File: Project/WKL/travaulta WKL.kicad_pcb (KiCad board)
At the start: 4 copper layers, 208.3 x 75.8 mm, 107 parts, among them J1 ARGB, SW1 EC_SW, SW10 EC_SW, SW11 EC_SW, SW12 EC_SW, SW13 EC_SW, SW14 EC_SW, SW15 EC_SW, SW16 EC_SW, SW17 EC_SW, SW18 EC_SW, SW19 EC_SW, SW2 EC_SW, SW20 EC_SW, SW21 EC_SW, SW22 EC_SW, SW23 EC_SW, SW24 EC_SW, SW25 EC_SW, SW26 EC_SW, SW27 EC_SW, SW28 EC_SW, SW29 EC_SW, SW3 EC_SW, SW30 EC_SW, SW31 EC_SW, SW32 EC_SW, SW33 EC_SW, SW34 EC_SW, SW35 EC_SW, SW36 EC_SW, SW37 EC_SW, SW38 BOOT0, SW4 EC_SW, SW5 EC_SW, SW6 EC_SW, SW7 EC_SW, SW8 EC_SW, SW9 EC_SW, U1 STM32F401CBUx, U2 XC6206PxxxMR, U3 74HC4051, U4 74HC4051, U5 OPA350, Y1 8 MHz

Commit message: backup
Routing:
- net GND: track 46.9 -> 54.4 mm, vias 435 -> 431
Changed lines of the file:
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@@
   (via (at 163.576 76.2) (size 0.8) (drill 0.4) (layers "F.Cu" "B.Cu") (net 1))
   (via (at 195.012249 65.997905) (size 0.8) (drill 0.4) (layers "F.Cu" "B.Cu") (free) (net 1))
-  (via (at 153.288724 110.807639) (size 0.8) (drill 0.4) (layers "F.Cu" "B.Cu") (net 1))
   (via (at 111.531688 103.066962) (size 0.8) (drill 0.4) (layers "F.Cu" "B.Cu") (free) (net 1))
   (via (at 71.700833 102.228857) (size 0.8) (drill 0.4) (layers "F.Cu" "B.Cu") (free) (net 1))
@@
   (via (at 118.067619 104.395436) (size 0.8) (drill 0.4) (layers "F.Cu" "B.Cu") (free) (net 1))
   (via (at 223.514768 103.879942) (size 0.8) (drill 0.4) (layers "F.Cu" "B.Cu") (free) (net 1))
-  (via (at 150.5501 110.815963) (size 0.8) (drill 0.4) (layers "F.Cu" "B.Cu") (net 1))
   (via (at 78.556941 103.85914) (size 0.8) (drill 0.4) (layers "F.Cu" "B.Cu") (free) (net 1))
   (via (at 237.353345 102.760391) (size 0.8) (drill 0.4) (layers "F.Cu" "B.Cu") (free) (net 1))
@@
   (via (at 215.79072 65.997413) (size 0.8) (drill 0.4) (layers "F.Cu" "B.Cu") (free) (net 1))
   (via (at 139.953601 68.350091) (size 0.8) (drill 0.4) (layers "F.Cu" "B.Cu") (free) (net 1))
-  (via (at 153.346 115.062) (size 0.8) (drill 0.4) (layers "F.Cu" "B.Cu") (net 1))
   (via (at 87.653038 51.101306) (size 0.8) (drill 0.4) (layers "F.Cu" "B.Cu") (net 1))
   (via (at 84.074 69.85) (size 0.8) (drill 0.4) (layers "F.Cu" "B.Cu") (free) (net 1))
   (via (at 151.425252 121.036363) (size 0.8) (drill 0.4) (layers "F.Cu" "B.Cu") (free) (net 1))
   (via (at 184.94375 106.3625) (size 0.8) (drill 0.4) (layers "F.Cu" "B.Cu") (net 1))
-  (via (at 150.425 115.062) (size 0.8) (drill 0.4) (layers "F.Cu" "B.Cu") (net 1))
   (segment (start 85.75 53.624) (end 86.81 53.624) (width 0.25) (layer "B.Cu") (net 1))
   (segment (start 157.41 114.683) (end 158.047 114.683) (width 0.25) (layer "B.Cu") (net 1))
   (segment (start 86.81 53.624) (end 87.67 52.764) (width 0.25) (layer "B.Cu") (net 1))
+  (segment (start 154.904 109.4655) (end 154.904 110.653) (width 0.25) (layer "B.Cu") (net 1))
   (segment (start 86.87 50.318268) (end 86.87 48.44375) (width 0.25) (layer "B.Cu") (net 1))
   (segment (start 87.653038 51.101306) (end 86.87 50.318268) (width 0.25) (layer "B.Cu") (net 1))
@@
   (segment (start 77.43 52.764) (end 77.43 51.094) (width 0.25) (layer "B.Cu") (net 1))
   (segment (start 151.896 116.3405) (end 151.896 113.591) (width 0.25) (layer "B.Cu") (net 1))
-  (segment (start 154.851186 115.15718) (end 154.701186 115.00718) (width 0.25) (layer "B.Cu") (net 1))
   (segment (start 78.29 53.624) (end 77.43 52.764) (width 0.25) (layer "B.Cu") (net 1))
   (segment (start 149.04 118.491) (end 149.031 118.5) (width 0.25) (layer "B.Cu") (net 1))
   (segment (start 188.33834 107.55242) (end 188.33834 106.58209) (width 0.25) (layer "B.Cu") (net 1))
   (segment (start 82.903 69.85) (end 84.074 69.85) (width 0.25) (layer "B.Cu") (net 1))
-  (segment (start 154.889279 109.405399) (end 154.889279 110.592899) (width 0.25) (layer "B.Cu") (net 1))
   (segment (start 77.77875 48.895) (end 75.692 48.895) (width 0.25) (layer "B.Cu") (net 1))
   (segment (start 188.33834 106.58209) (end 188.08319 106.32694) (width 0.25) (layer "B.Cu") (net 1))
@@
   (segment (start 77.43 51.094) (end 78.23 50.294) (width 0.25) (layer "B.Cu") (net 1))
   (segment (start 84.201 56.35625) (end 84.201 57.283328) (width 0.25) (layer "B.Cu") (net 1))
-  (segment (start 150.4001 110.665963) (end 150.5501 110.815963) (width 0.25) (layer "B.Cu") (net 1))
+  (segment (start 156.0915 115.153) (end 154.904 115.153) (width 0.25) (layer "B.Cu") (net 1))
   (segment (start 187.12434 106.32694) (end 184.97931 106.32694) (width 0.25) (layer "B.Cu") (net 1))
   (segment (start 151.896 116.3405) (end 151.896 118.233) (width 0.25) (layer "B.Cu") (net 1))
   (segment (start 78.23 50.294) (end 78.23 48.44375) (width 0.25) (layer "B.Cu") (net 1))
+  (segment (start 149.2165 110.653) (end 150.334 110.653) (width 0.25) (layer "B.Cu") (net 1))
   (segment (start 187.12434 107.62742) (end 188.26334 107.62742) (width 0.25) (layer "B.Cu") (net 1))
   (segment (start 79.35 53.624) (end 78.29 53.624) (width 0.25) (layer "B.Cu") (net 1))
@@
   (segment (start 87.67 52.764) (end 87.67 51.118268) (width 0.25) (layer "B.Cu") (net 1))
   (segment (start 158.299 115.635994) (end 158.271 115.663994) (width 0.25) (layer "B.Cu") (net 1))
-  (segment (start 150.5501 110.815963) (end 150.387137 110.653) (width 0.25) (layer "B.Cu") (net 1))
   (segment (start 78.23 48.44375) (end 77.77875 48.895) (width 0.25) (layer "B.Cu") (net 1))
+  (segment (start 154.904 110.653) (end 152.654 112.903) (width 0.25) (layer "B.Cu") (net 1))
   (segment (start 184.97931 106.32694) (end 184.94375 106.3625) (width 0.25) (layer "B.Cu") (net 1))
   (segment (start 87.32125 48.895) (end 89.408 48.895) (width 0.25) (layer "B.Cu") (net 1))
-  (segment (start 156.038686 115.15718) (end 154.851186 115.15718) (width 0.25) (layer "B.Cu") (net 1))
+  (segment (start 154.904 115.153) (end 152.654 112.903) (width 0.25) (layer "B.Cu") (net 1))
   (segment (start 188.26334 107.62742) (end 188.33834 107.55242) (width 0.25) (layer "B.Cu") (net 1))
   (segment (start 151.896 118.233) (end 151.638 118.491) (width 0.25) (layer "B.Cu") (net 1))
-  (segment (start 154.889279 110.592899) (end 154.739279 110.742899) (width 0.25) (layer "B.Cu") (net 1))
+  (segment (start 150.334 110.653) (end 152.584 112.903) (width 0.25) (layer "B.Cu") (net 1))
   (segment (start 151.638 118.491) (end 149.04 118.491) (width 0.25) (layer "B.Cu") (net 1))
   (segment (start 158.299 114.935) (end 158.047 114.683) (width 0.25) (layer "B.Cu") (net 1))
-  (segment (start 149.2126 110.665963) (end 150.4001 110.665963) (width 0.25) (layer "B.Cu") (net 1))
   (segment (start 84.201 57.283328) (end 84.198075 57.286253) (width 0.25) (layer "B.Cu") (net 1))
-  (segment (start 150.387137 110.653) (end 149.2165 110.653) (width 0.25) (layer "B.Cu") (net 1))
   (segment (start 155.409314 107.55) (end 154.3875 107.55) (width 0.2) (layer "B.Cu") (net 2))
   (segment (start 81.8 54.474) (end 82.063 54.737) (width 0.2) (layer "B.Cu") (net 2))

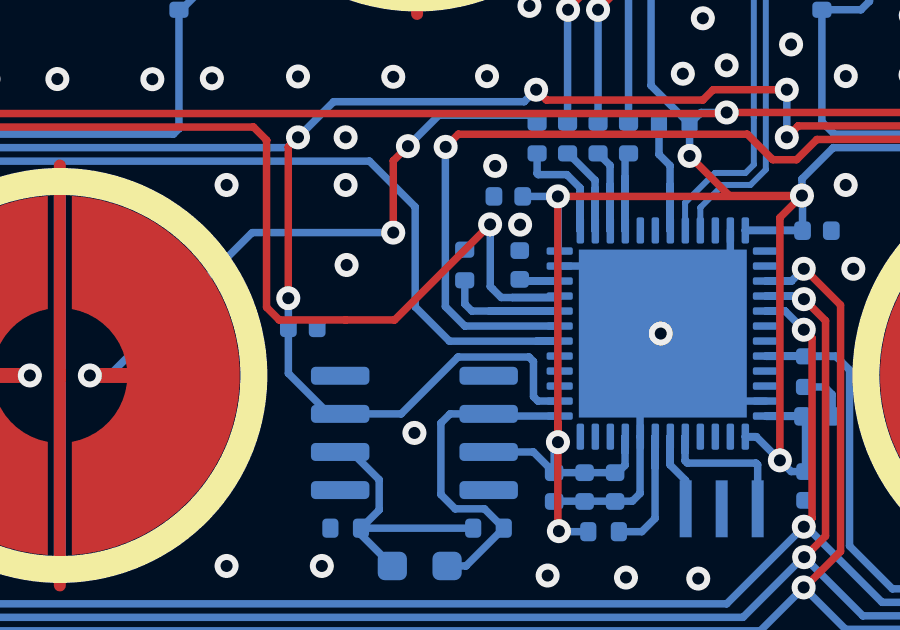
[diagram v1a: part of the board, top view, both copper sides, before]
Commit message: changed rgb pin on HHKB&WKL for better compatibility
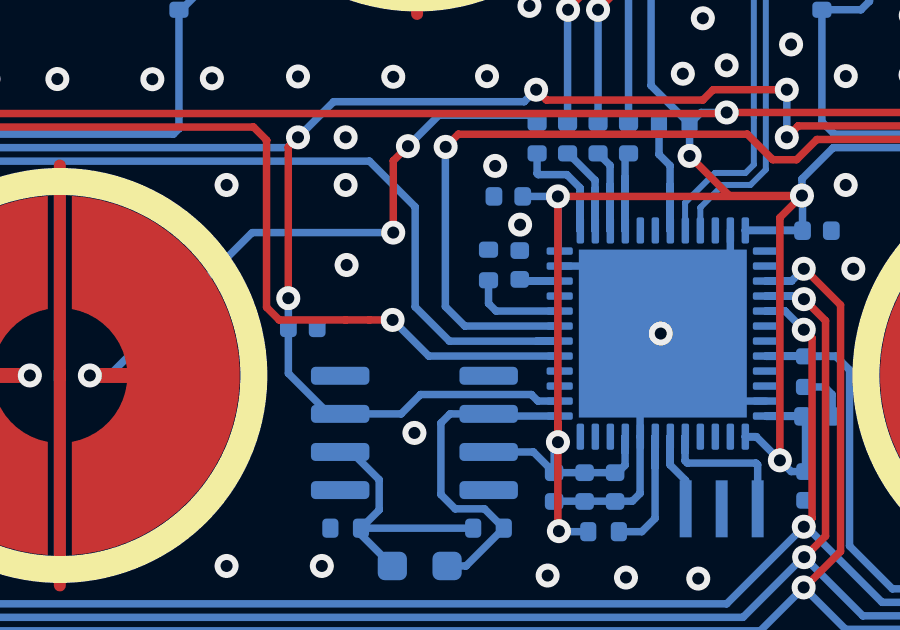
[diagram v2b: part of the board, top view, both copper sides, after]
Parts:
- moved R7 0.79 mm to (146.8, 110.6)
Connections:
- U1 pad 17: unconnected-(U1-PA7-Pad17) -> RGB
- U1 pad 21: RGB -> unconnected-(U1-PB10-Pad21)
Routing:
- net RGB: track 99.5 -> 94.6 mm
- net BOOT1: track 6.39 -> 3.25 mm
- net APLEX_OUT_PIN_0: track 94.2 -> 92.5 mm
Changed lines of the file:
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@@
   (net 59 "unconnected-(U1-PA5-Pad15)")
   (net 60 "unconnected-(U1-PA6-Pad16)")
-  (net 61 "unconnected-(U1-PA7-Pad17)")
+  (net 61 "unconnected-(U1-PB10-Pad21)")
   (net 62 "unconnected-(U1-PB7-Pad43)")
   (net 63 "COL10")
@@
   )
   (footprint "Resistor_SMD:R_0402_1005Metric" (layer "B.Cu")
-    (at 146.05 110.617 -90)
+    (at 146.84375 110.617 -90)
     (descr "Resistor SMD 0402 (1005 Metric), square (rectangular) end terminal, IPC_7351 nominal, (Body size source: IPC-SM-782 page 72, https://www.pcb-3d.com/wordpress/wp-content/uploads/ipc-sm-782a_amendment_1_and_2.pdf), generated with kicad-footprint-generator")
     (tags "resistor")
@@
       (net 60 "unconnected-(U1-PA6-Pad16)") (pinfunction "PA6") (pintype "bidirectional+no_connect"))
     (pad "17" smd roundrect (at -0.75 -3.4375 90) (size 0.25 0.875) (layers "B.Cu" "B.Paste" "B.Mask") (roundrect_rratio 0.25)
-      (net 61 "unconnected-(U1-PA7-Pad17)") (pinfunction "PA7") (pintype "bidirectional+no_connect"))
+      (net 51 "RGB") (pinfunction "PA7") (pintype "bidirectional"))
     (pad "18" smd roundrect (at -0.25 -3.4375 90) (size 0.25 0.875) (layers "B.Cu" "B.Paste" "B.Mask") (roundrect_rratio 0.25)
       (net 48 "APLEX_EN_PIN_0") (pinfunction "PB0") (pintype "bidirectional"))
@@
       (net 13 "BOOT1") (pinfunction "PB2") (pintype "bidirectional"))
     (pad "21" smd roundrect (at 1.25 -3.4375 90) (size 0.25 0.875) (layers "B.Cu" "B.Paste" "B.Mask") (roundrect_rratio 0.25)
-      (net 51 "RGB") (pinfunction "PB10") (pintype "bidirectional"))
+      (net 61 "unconnected-(U1-PB10-Pad21)") (pinfunction "PB10") (pintype "bidirectional+no_connect"))
     (pad "22" smd roundrect (at 1.75 -3.4375 90) (size 0.25 0.875) (layers "B.Cu" "B.Paste" "B.Mask") (roundrect_rratio 0.25)
       (net 6 "Net-(U1-VCAP1)") (pinfunction "VCAP1") (pintype "power_in"))
@@
   (segment (start 119.0625 106.70625) (end 140.15 106.70625) (width 0.25) (layer "B.Cu") (net 8))
   (segment (start 141.68125 105.175) (end 148.03125 105.175) (width 0.25) (layer "B.Cu") (net 8))
-  (segment (start 148.342847 113.834251) (end 148.342847 115.005347) (width 0.25) (layer "B.Cu") (net 8))
+  (segment (start 144.577345 114.935501) (end 143.932346 115.580501) (width 0.25) (layer "B.Cu") (net 8))
   (segment (start 140.1725 112.7125) (end 140.1725 111.728779) (width 0.25) (layer "B.Cu") (net 8))
-  (segment (start 148.4905 115.153) (end 149.2165 115.153) (width 0.25) (layer "B.Cu") (net 8))
   (segment (start 187.12434 106.97718) (end 185.91657 106.97718) (width 0.25) (layer "B.Cu") (net 8))
   (segment (start 140.49375 106.3625) (end 141.68125 105.175) (width 0.25) (layer "B.Cu") (net 8))
-  (segment (start 145.827346 113.685501) (end 148.194097 113.685501) (width 0.25) (layer "B.Cu") (net 8))
-  (segment (start 141.899097 115.580501) (end 143.932346 115.580501) (width 0.25) (layer "B.Cu") (net 8))
   (segment (start 117.27434 106.97718) (end 118.79157 106.97718) (width 0.25) (layer "B.Cu") (net 8))
   (segment (start 185.91657 106.97718) (end 184.94375 107.95) (width 0.25) (layer "B.Cu") (net 8))
-  (segment (start 148.194097 113.685501) (end 148.342847 113.834251) (width 0.25) (layer "B.Cu") (net 8))
+  (segment (start 148.4905 115.153) (end 148.273001 114.935501) (width 0.25) (layer "B.Cu") (net 8))
+  (segment (start 149.2165 115.153) (end 148.4905 115.153) (width 0.25) (layer "B.Cu") (net 8))
   (segment (start 140.15 106.70625) (end 140.49375 106.3625) (width 0.25) (layer "B.Cu") (net 8))
   (segment (start 148.03125 105.175) (end 148.43125 104.775) (width 0.25) (layer "B.Cu") (net 8))
+  (segment (start 148.273001 114.935501) (end 144.577345 114.935501) (width 0.25) (layer "B.Cu") (net 8))
   (segment (start 140.1725 111.728779) (end 140.168917 111.725196) (width 0.25) (layer "B.Cu") (net 8))
   (segment (start 141.899097 115.580501) (end 141.522346 115.580501) (width 0.25) (layer "B.Cu") (net 8))
-  (segment (start 148.342847 115.005347) (end 148.4905 115.153) (width 0.25) (layer "B.Cu") (net 8))
+  (segment (start 143.932346 115.580501) (end 141.899097 115.580501) (width 0.25) (layer "B.Cu") (net 8))
   (segment (start 141.522346 115.580501) (end 140.1725 114.230655) (width 0.25) (layer "B.Cu") (net 8))
-  (segment (start 143.932346 115.580501) (end 145.827346 113.685501) (width 0.25) (layer "B.Cu") (net 8))
   (segment (start 156.787 106.3625) (end 156.787 104.775) (width 0.25) (layer "B.Cu") (net 8))
   (segment (start 140.1725 114.230655) (end 140.1725 112.7125) (width 0.25) (layer "B.Cu") (net 8))
@@
   (segment (start 153.929791 105.533209) (end 153.545 105.918) (width 0.25) (layer "B.Cu") (net 12))
   (segment (start 157.311 109.474) (end 157.311 108.322143) (width 0.25) (layer "B.Cu") (net 12))
-  (segment (start 146.881 112.153) (end 149.2165 112.153) (width 0.25) (layer "B.Cu") (net 13))
-  (segment (start 146.054312 111.918661) (end 146.054312 111.126911) (width 0.25) (layer "B.Cu") (net 13))
-  (segment (start 146.288562 112.152911) (end 146.054312 111.918661) (width 0.25) (layer "B.Cu") (net 13))
-  (segment (start 147.641812 112.152911) (end 146.288562 112.152911) (width 0.25) (layer "B.Cu") (net 13))
-  (segment (start 147.641812 112.152911) (end 149.220812 112.152911) (width 0.25) (layer "B.Cu") (net 13))
+  (segment (start 146.84375 111.899958) (end 147.096792 112.153) (width 0.25) (layer "B.Cu") (net 13))
+  (segment (start 147.096792 112.153) (end 149.2165 112.153) (width 0.25) (layer "B.Cu") (net 13))
+  (segment (start 146.84375 111.127) (end 146.84375 111.899958) (width 0.25) (layer "B.Cu") (net 13))
   (via (at 59.53125 114.3) (size 0.8) (drill 0.4) (layers "F.Cu" "B.Cu") (net 14))
   (via (at 62.103 95.25) (size 0.8) (drill 0.4) (layers "F.Cu" "B.Cu") (net 14))
@@
   (segment (start 117.27434 108.92282) (end 118.37265 108.92282) (width 0.25) (layer "B.Cu") (net 48))
   (segment (start 108.293839 107.95) (end 106.659368 106.31553) (width 0.25) (layer "F.Cu") (net 51))
+  (segment (start 143.647122 112.448643) (end 142.876464 112.448643) (width 0.25) (layer "F.Cu") (net 51))
   (segment (start 76.521271 92.075) (end 74.326714 92.075) (width 0.25) (layer "F.Cu") (net 51))
   (segment (start 113.547244 106.018661) (end 111.615905 107.95) (width 0.25) (layer "F.Cu") (net 51))
   (segment (start 77.44398 103.062865) (end 76.980307 102.599192) (width 0.25) (layer "F.Cu") (net 51))
+  (segment (start 142.876464 112.448643) (end 142.875 112.450107) (width 0.25) (layer "F.Cu") (net 51))
   (segment (start 106.659368 106.31553) (end 96.160076 106.31553) (width 0.25) (layer "F.Cu") (net 51))
   (segment (start 139.448229 106.457609) (end 139.009281 106.018661) (width 0.25) (layer "F.Cu") (net 51))
@@
   (segment (start 139.443917 106.461921) (end 139.448229 106.457609) (width 0.25) (layer "F.Cu") (net 51))
   (segment (start 92.907411 103.062865) (end 77.44398 103.062865) (width 0.25) (layer "F.Cu") (net 51))
-  (segment (start 146.901419 109.263689) (end 143.715001 112.450107) (width 0.25) (layer "F.Cu") (net 51))
   (segment (start 76.980307 92.534036) (end 76.521271 92.075) (width 0.25) (layer "F.Cu") (net 51))
   (segment (start 139.443917 112.025501) (end 139.443917 106.461921) (width 0.25) (layer "F.Cu") (net 51))
   (segment (start 96.160076 106.31553) (end 92.907411 103.062865) (width 0.25) (layer "F.Cu") (net 51))
   (segment (start 111.615905 107.95) (end 108.293839 107.95) (width 0.25) (layer "F.Cu") (net 51))
+  (segment (start 142.875 112.450107) (end 142.08125 112.450107) (width 0.25) (layer "F.Cu") (net 51))
   (segment (start 142.08125 112.450107) (end 142.081161 112.450196) (width 0.25) (layer "F.Cu") (net 51))
   (segment (start 76.980307 102.599192) (end 76.980307 92.534036) (width 0.25) (layer "F.Cu") (net 51))
   (segment (start 142.081161 112.450196) (end 139.868612 112.450196) (width 0.25) (layer "F.Cu") (net 51))
-  (segment (start 143.715001 112.450107) (end 142.08125 112.450107) (width 0.25) (layer "F.Cu") (net 51))
-  (via (at 146.897108 109.263649) (size 0.8) (drill 0.4) (layers "F.Cu" "B.Cu") (net 51))
-  (segment (start 147.6375 111.701911) (end 147.266352 111.701911) (width 0.25) (layer "B.Cu") (net 51))
-  (segment (start 146.901419 111.336978) (end 146.901419 109.5375) (width 0.25) (layer "B.Cu") (net 51))
-  (segment (start 147.6375 111.701911) (end 149.167589 111.701911) (width 0.25) (layer "B.Cu") (net 51))
-  (segment (start 146.979449 111.415008) (end 146.901419 111.336978) (width 0.25) (layer "B.Cu") (net 51))
-  (segment (start 146.901419 109.5375) (end 146.901419 109.263689) (width 0.25) (layer "B.Cu") (net 51))
-  (segment (start 149.171812 111.701911) (end 147.6375 111.701911) (width 0.25) (layer "B.Cu") (net 51))
-  (segment (start 147.266352 111.701911) (end 146.979449 111.415008) (width 0.25) (layer "B.Cu") (net 51))
-  (segment (start 146.901419 109.26796) (end 146.897108 109.263649) (width 0.25) (layer "B.Cu") (net 51))
-  (segment (start 146.901419 109.5375) (end 146.901419 109.26796) (width 0.25) (layer "B.Cu") (net 51))
-  (segment (start 149.167589 111.701911) (end 149.2165 111.653) (width 0.25) (layer "B.Cu") (net 51))
+  (via (at 143.647122 112.448643) (size 0.8) (drill 0.4) (layers "F.Cu" "B.Cu") (net 51))
+  (segment (start 149.2165 113.653) (end 144.851479 113.653) (width 0.25) (layer "B.Cu") (net 51))
+  (segment (start 144.851479 113.653) (end 143.647122 112.448643) (width 0.25) (layer "B.Cu") (net 51))
   (via (at 245.491 57.15) (size 0.8) (drill 0.4) (layers "F.Cu" "B.Cu") (net 63))
   (via (at 250.878697 100.53016) (size 0.8) (drill 0.4) (layers "F.Cu" "B.Cu") (net 63))

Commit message: fresh gerbers for HHKB WKL
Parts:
- added G***: LOGO, LOGO, B.Cu at (246.9, 73.8)
- moved G*** 0.79 mm to (250.8, 82.5)
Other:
- board text added: "by Calvin0563"
- board text removed: "by Calvin0563 for mechvault's vault35"
